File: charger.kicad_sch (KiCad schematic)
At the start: 21 parts, among them J1 USB_C_PD, Q2 DUAL_N_FET, U2 CH224K, U3 BQ24650

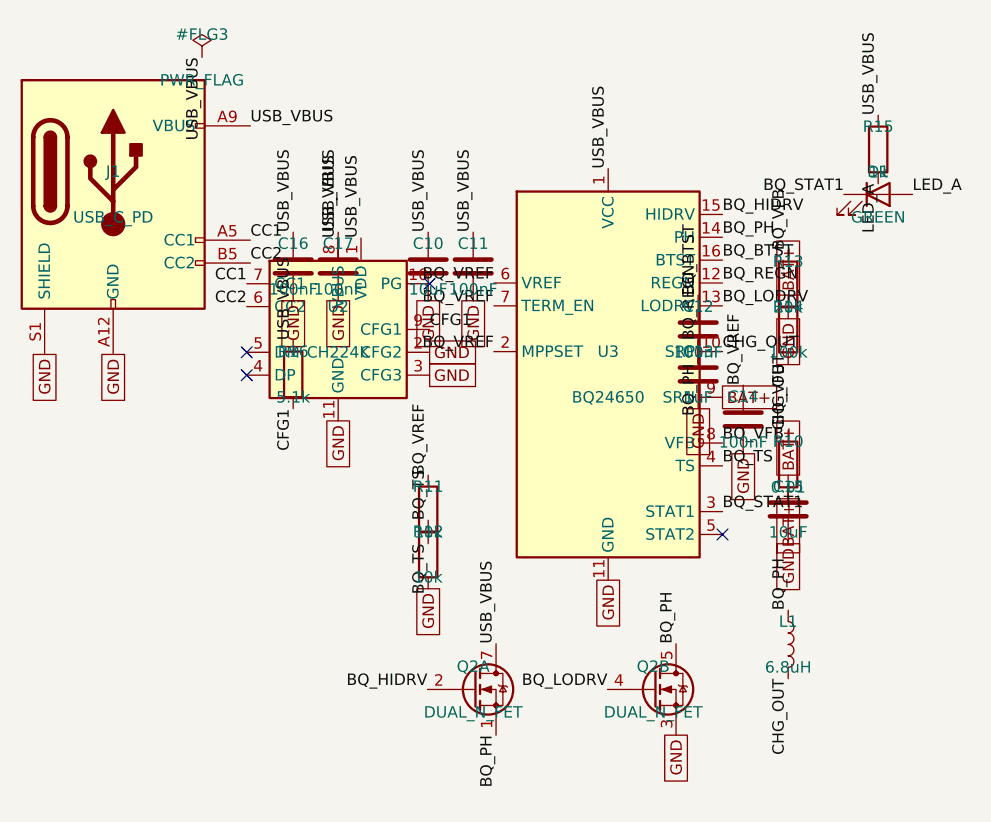
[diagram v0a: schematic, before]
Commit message: schematic: parts pass + cell-holder and USB-C symbol swaps
- Apply Footprint + LCSC + Description to all 67 non-cell components
  across bms / charger / buckboost (JLCPCB-friendly BOM).
- Add project-local power_module_lib (symbols + footprints fetched via
  easyeda2kicad for BH-18650-B5BA016 holder and the two custom-package
  inductors).
- bms: replace BT1-3 (3x Battery_Cell) with single 6-pin BAT1 holder
  (BH-18650-B5BA016, C19184086). Pin mapping respects all-cells-same-
  direction; CELL1_TOP/CELL2_TOP taps repeat on inner pins.
- charger: swap J1 from USB_C_Receptacle_PowerOnly_24P to
  USB_C_Receptacle_USB2.0_16P (matches HRO TYPE-C-31-M-12 16P
  footprint). NC the 6 unused USB 2.0 data + SBU pins.
- R21 value 90k -> 91k (E96 standard so 0603 1% available at JLC).
- ERC on charger dropped 9 -> 2 (remaining: pre-existing Input Power
  flag, plus harmless 'fp-lib-table missing' warning resolved at
  project scope).

Co-Authored-By: Claude Opus 4.7 <noreply@anthropic.com>
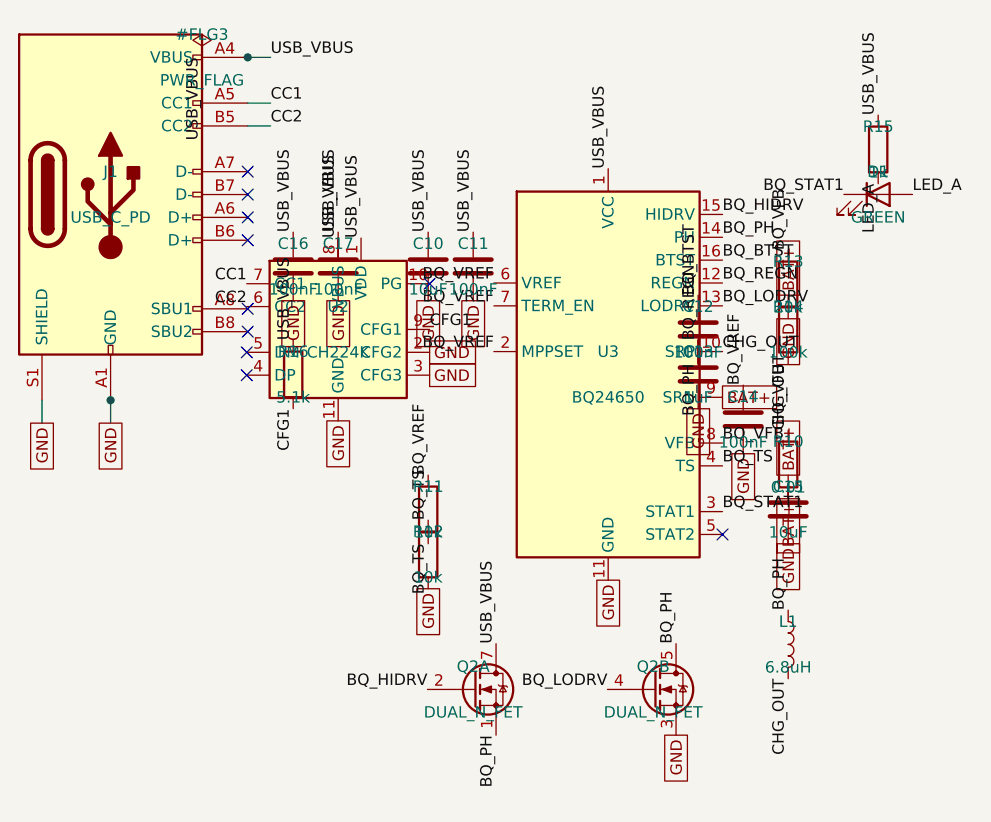
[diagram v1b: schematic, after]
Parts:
- removed J1: USB_C_PD, Connector_USB:USB_C_Receptacle_HRO_TYPE-C-31-M-12, symbol Connector:USB_C_Receptacle_PowerOnly_24P
- added J1: USB_C_PD, Connector_USB:USB_C_Receptacle_HRO_TYPE-C-31-M-12, symbol Connector:USB_C_Receptacle_USB2.0_16P
- C10, C15: footprint (none) -> Capacitor_SMD:C_0805_2012Metric; LCSC (none) -> C15850
- C11, C12, C14, C16, C17: footprint (none) -> Capacitor_SMD:C_0603_1608Metric; LCSC (none) -> C14663
- C13: footprint (none) -> Capacitor_SMD:C_0805_2012Metric; LCSC (none) -> C28323
- D1: LCSC (none) -> C2297
- L1: footprint Inductor_SMD:L_Bourns_SRR1280 -> power_module_lib:IND-SMD_L7.0-W6.6; LCSC (none) -> C167221
- Q2: footprint (none) -> Package_SO:SOIC-8_3.9x4.9mm_P1.27mm; LCSC (none) -> C353066
- R10: footprint Resistor_SMD:R_2512_6332Metric -> Resistor_SMD:R_1206_3216Metric; LCSC (none) -> C601097
- R11, R12: footprint (none) -> Resistor_SMD:R_0603_1608Metric; LCSC (none) -> C25804
- R13: footprint (none) -> Resistor_SMD:R_0603_1608Metric; LCSC (none) -> C4184
- R14: footprint (none) -> Resistor_SMD:R_0603_1608Metric; LCSC (none) -> C25803
- R15: footprint (none) -> Resistor_SMD:R_0603_1608Metric; LCSC (none) -> C21190
- R16: footprint (none) -> Resistor_SMD:R_0603_1608Metric; LCSC (none) -> C23186
- U2: footprint Package_SO:SSOP-10-1EP_3.9x4.9mm_P1mm_EP2.1x3.3mm -> Package_SO:MSOP-10_3x3mm_P0.5mm; LCSC (none) -> C970725
- U3: footprint Package_DFN_QFN:Texas_RVA_VQFN-16-1EP_3.5x3.5mm_P0.5mm_EP2.14x2.14mm_ThermalVias -> Package_DFN_QFN:QFN-16-1EP_3x3mm_P0.5mm_EP1.7x1.7mm; LCSC (none) -> C53712
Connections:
- net CC1: now also J1.A5 (CC1)
- net CC2: now also J1.B5 (CC2)
- net GND: now also J1.A1 (GND), J1.A12 (GND), J1.B1 (GND), J1.B12 (GND), J1.S1 (SHIELD)
- net USB_VBUS: now also J1.A4 (VBUS), J1.A9 (VBUS), J1.B4 (VBUS), J1.B9 (VBUS)
- no-connect marks 4 -> 10
